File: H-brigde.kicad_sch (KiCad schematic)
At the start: 17 parts, among them J201 track out, J202 track out, U201 L298N

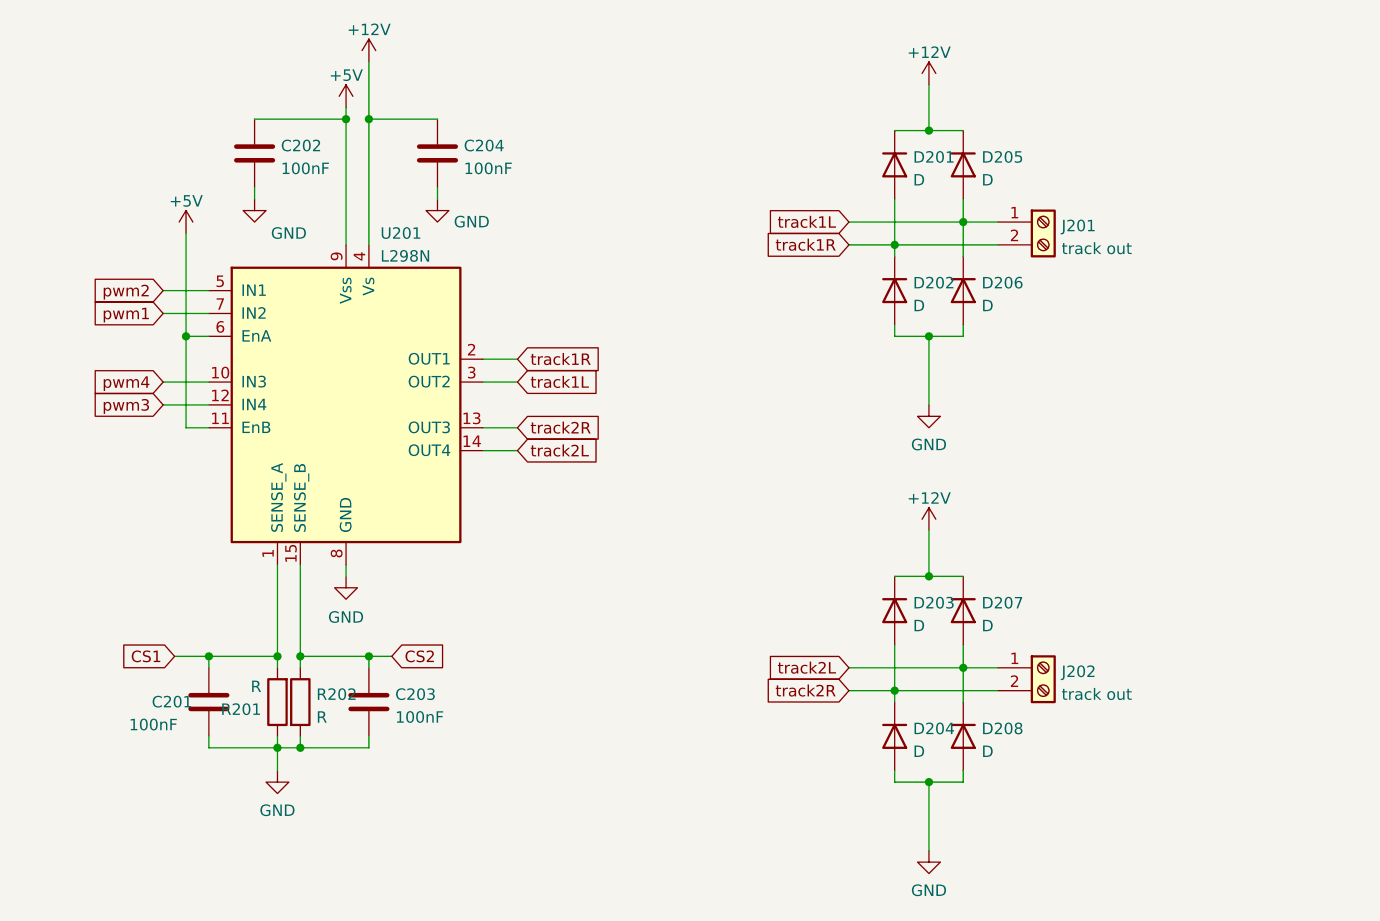
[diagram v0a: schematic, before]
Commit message: altered the code drastically and made a new PCB. PCB is still much work.
I finally fixed that issue where loco functions and speed were not serviced to the multimaus clients.
The Nx code also has been succesfully tested using the monitor.
MCP bug also has been solded. The bug was in assembleIO.py
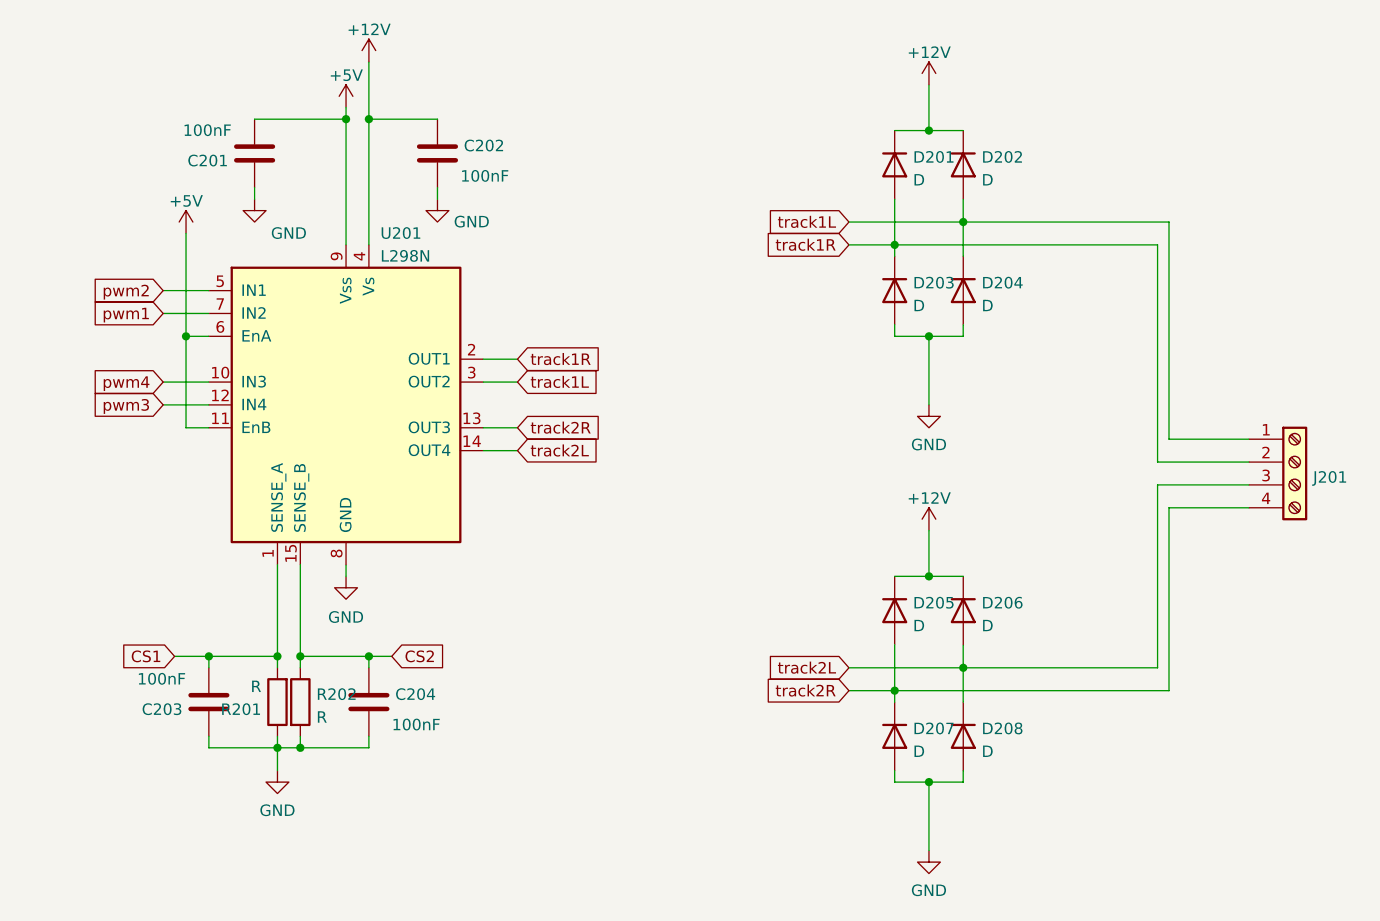
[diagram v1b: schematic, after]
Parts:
- removed J201, J202: track out, TerminalBlock_Phoenix:TerminalBlock_Phoenix_MKDS-1,5-2-5.08_1x02_P5.08mm_Horizontal, symbol Connector:Screw_Terminal_01x02
- added J201: (no value), symbol Connector:Screw_Terminal_01x04
- C201, C202, C203, C204: footprint Capacitor_THT:C_Disc_D3.0mm_W1.6mm_P2.50mm -> Capacitor_SMD:C_0603_1608Metric_Pad1.08x0.95mm_HandSolder; JLCPCB Part# (none) -> C14663
- D201, D202, D203, D204, D205, D206, D207, D208: footprint Diode_THT:D_DO-34_SOD68_P7.62mm_Horizontal -> Diode_SMD:D_SMA_Handsoldering; JLCPCB Part# (none) -> C95872
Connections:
- net +12V: now also C202.1, D202.1 (K), D206.1 (K); no longer C204.1, D203.1 (K), D207.1 (K)
- net +5V: now also C201.2; no longer C202.1
- net CS1: now also C203.2; no longer C201.2
- net CS2: now also C204.1; no longer C203.1
- net GND: now also C203.1, D203.2 (A), D207.2 (A); no longer C203.2, D202.2 (A), D206.2 (A)
- net track1L: now also D202.2 (A), D204.1 (K), J201.1 (Pin_1); no longer D205.2 (A), D206.1 (K)
- net track1R: now also D203.1 (K), J201.2 (Pin_2); no longer D202.1 (K)
- net track2L: now also D206.2 (A), J201.3 (Pin_3); no longer D207.2 (A)
- net track2R: now also D205.2 (A), D207.1 (K), J201.4 (Pin_4); no longer D203.2 (A), D204.1 (K)

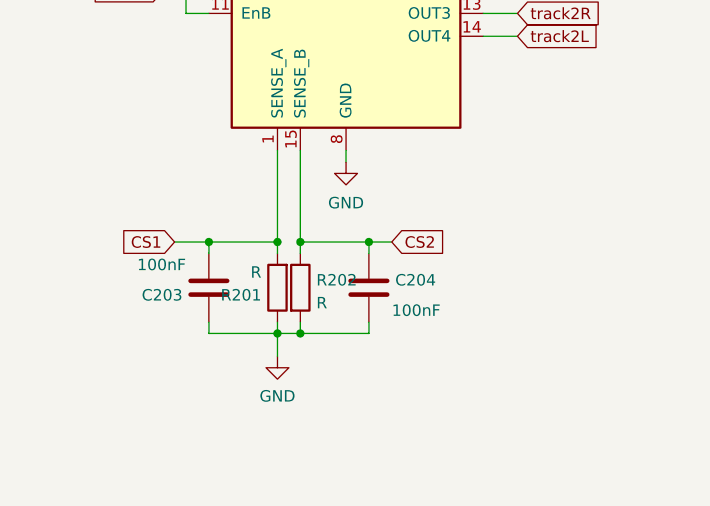
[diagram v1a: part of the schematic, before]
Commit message: added missing schematics
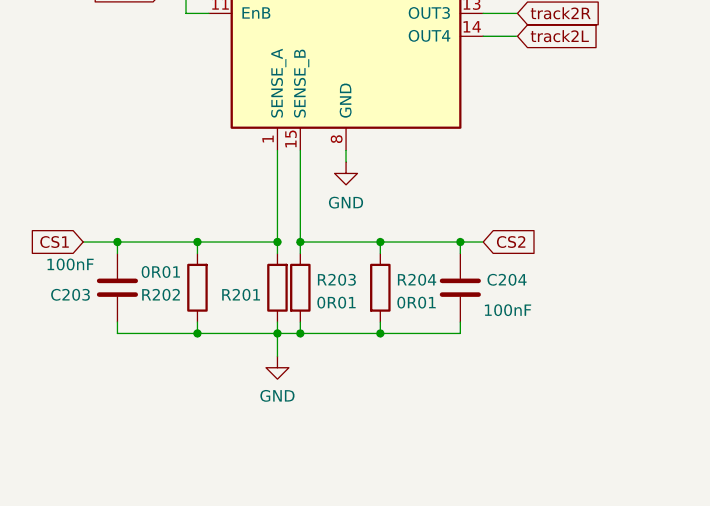
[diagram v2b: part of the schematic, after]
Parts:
- added R203, R204: 0R01, Resistor_SMD:R_1206_3216Metric_Pad1.30x1.75mm_HandSolder, symbol Device:R
- J201: value (none) -> Screw_Terminal_01x04; footprint (none) -> TerminalBlock_Phoenix:TerminalBlock_Phoenix_MKDS-1,5-4-5.08_1x04_P5.08mm_Horizontal
- R201: value R -> (none); footprint Resistor_THT:R_Axial_DIN0516_L15.5mm_D5.0mm_P20.32mm_Horizontal -> (none); JLCPCB Part# (none) -> C25334
- R202: value R -> 0R01; footprint Resistor_THT:R_Axial_DIN0516_L15.5mm_D5.0mm_P20.32mm_Horizontal -> Resistor_SMD:R_1206_3216Metric_Pad1.30x1.75mm_HandSolder; JLCPCB Part# (none) -> C25334
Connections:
- net CS1: now also R202.2
- net CS2: now also R203.1, R204.1; no longer R202.1
- net GND: now also R202.1, R203.2, R204.2; no longer R202.2
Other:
- moved on the sheet: C203, C204

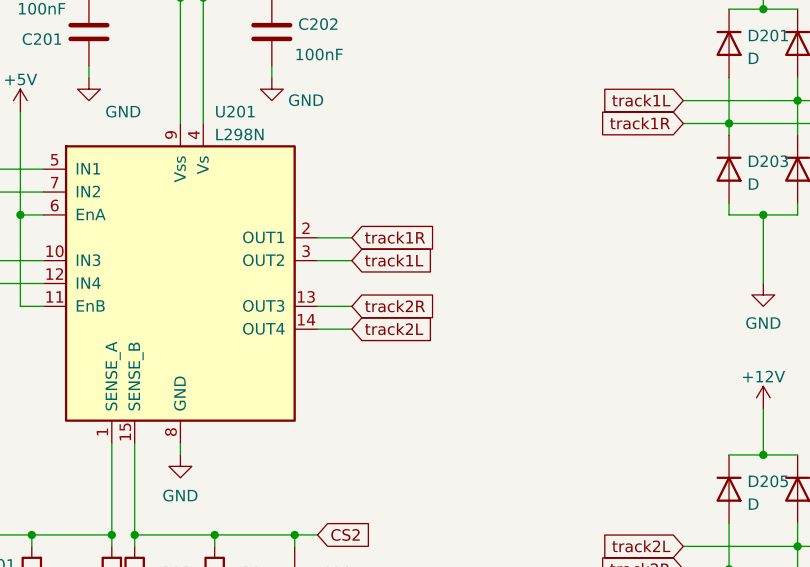
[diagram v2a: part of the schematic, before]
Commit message: replaced the atmega2560 by an stm32
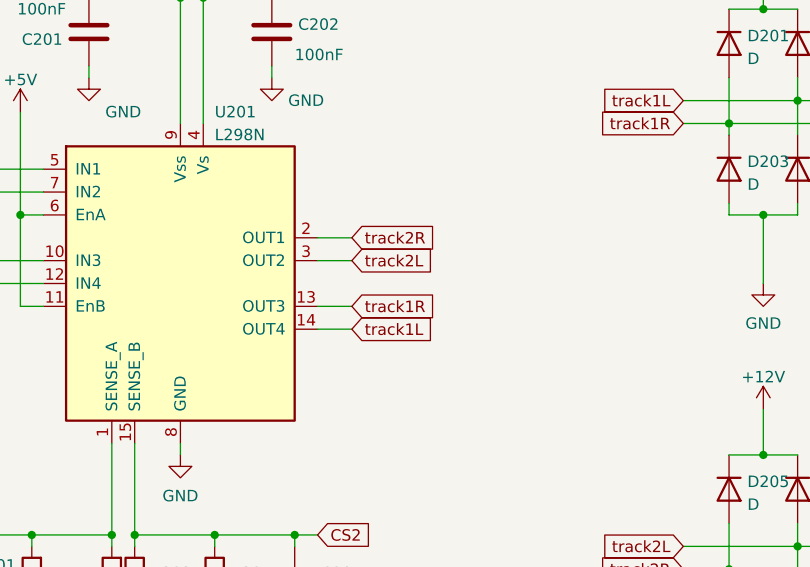
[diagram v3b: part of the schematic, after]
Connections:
- net track1L: now also U201.14 (OUT4); no longer U201.3 (OUT2)
- net track1R: now also U201.13 (OUT3); no longer U201.2 (OUT1)
- net track2L: now also U201.3 (OUT2); no longer U201.14 (OUT4)
- net track2R: now also U201.2 (OUT1); no longer U201.13 (OUT3)
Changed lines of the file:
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@@
     )
   )
-  (global_label "track1R" (shape input) (at 142.24 91.44 0) (fields_autoplaced)
+  (global_label "track1R" (shape input) (at 142.24 99.06 0) (fields_autoplaced)
     (effects (font (size 1.27 1.27)) (justify left))
-    (property "Intersheet References" "${INTERSHEET_REFS}" (id 0) (at 151.9102 91.5194 0)
+    (property "Intersheet References" "${INTERSHEET_REFS}" (id 0) (at 151.9102 99.1394 0)
       (effects (font (size 1.27 1.27)) (justify left) hide)
     )
@@
     )
   )
-  (global_label "track1L" (shape input) (at 142.24 93.98 0) (fields_autoplaced)
+  (global_label "track1L" (shape input) (at 142.24 101.6 0) (fields_autoplaced)
     (effects (font (size 1.27 1.27)) (justify left))
-    (property "Intersheet References" "${INTERSHEET_REFS}" (id 0) (at 151.6683 94.0594 0)
+    (property "Intersheet References" "${INTERSHEET_REFS}" (id 0) (at 151.6683 101.6794 0)
       (effects (font (size 1.27 1.27)) (justify left) hide)
     )
@@
     )
   )
-  (global_label "track2L" (shape input) (at 142.24 101.6 0) (fields_autoplaced)
+  (global_label "track2L" (shape input) (at 142.24 93.98 0) (fields_autoplaced)
     (effects (font (size 1.27 1.27)) (justify left))
-    (property "Intersheet References" "${INTERSHEET_REFS}" (id 0) (at 151.6683 101.6794 0)
+    (property "Intersheet References" "${INTERSHEET_REFS}" (id 0) (at 151.6683 94.0594 0)
       (effects (font (size 1.27 1.27)) (justify left) hide)
     )
@@
     )
   )
-  (global_label "track2R" (shape input) (at 142.24 99.06 0) (fields_autoplaced)
+  (global_label "track2R" (shape input) (at 142.24 91.44 0) (fields_autoplaced)
     (effects (font (size 1.27 1.27)) (justify left))
-    (property "Intersheet References" "${INTERSHEET_REFS}" (id 0) (at 151.9102 99.1394 0)
+    (property "Intersheet References" "${INTERSHEET_REFS}" (id 0) (at 151.9102 91.5194 0)
       (effects (font (size 1.27 1.27)) (justify left) hide)
     )
